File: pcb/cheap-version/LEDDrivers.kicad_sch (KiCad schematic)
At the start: 54 parts, among them J711 LED +/- (return isolated), J721 LED +/- (return isolated), J731 LED +/- (return isolated), Q711 BSC146N10LS5, Q721 BSC146N10LS5, U700 SN74LVC1G08DBVR, U710 AL8853S-13, U720 AL8853S-13

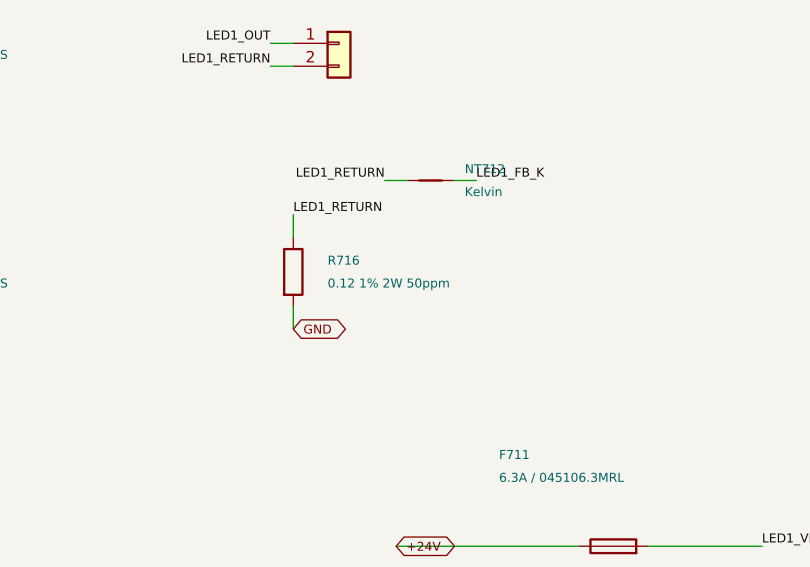
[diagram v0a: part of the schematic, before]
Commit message: Verify cheap-version purchase parts and require complete release checks
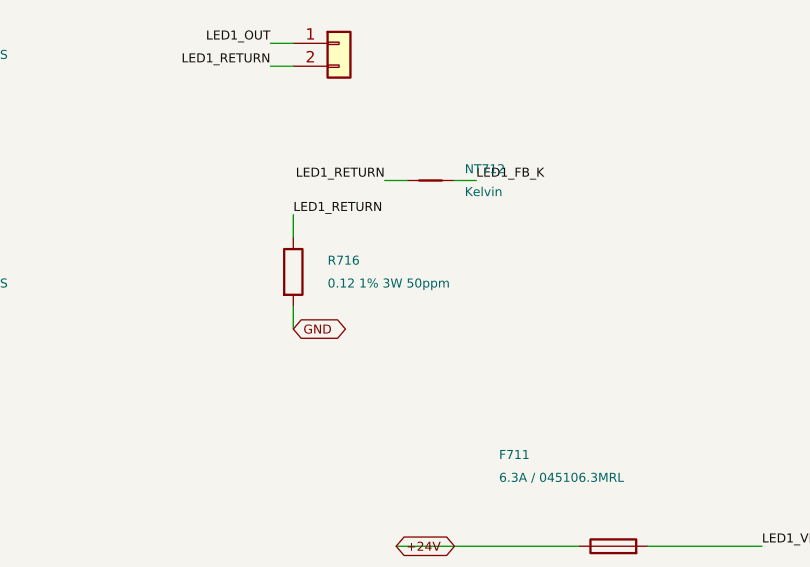
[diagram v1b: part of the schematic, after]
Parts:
- R716: value 0.12 1% 2W 50ppm -> 0.12 1% 3W 50ppm; LCSC (none) -> C49164917; MPN FRM252WFR120TM -> JER2512F3R120; Manufacturer FOJAN -> JIERR; Source (none) -> buy
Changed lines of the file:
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@@
 			)
 		)
-		(property "Value" "0.12 1% 2W 50ppm"
+		(property "Value" "0.12 1% 3W 50ppm"
 			(at 448.31 124.46 0)
 			(show_name no)
@@
 			)
 		)
-		(property "Datasheet" "https://datasheet.lcsc.com/datasheet/pdf/b47da348e6587de9f1f028172ba2b8ea.pdf"
+		(property "Datasheet" "https://datasheet.lcsc.com/datasheet/pdf/02ae4b20613551dea68a63964573e262.pdf"
 			(at 444.5 123.19 0)
 			(hide yes)
@@
 			)
 		)
-		(property "Manufacturer" "FOJAN"
+		(property "Manufacturer" "JIERR"
 			(at 444.5 123.19 0)
 			(hide yes)
@@
 			)
 		)
-		(property "MPN" "FRM252WFR120TM"
+		(property "MPN" "JER2512F3R120"
 			(at 444.5 123.19 0)
 			(hide yes)
@@
 			)
 		)
-		(property "LCSC" ""
+		(property "LCSC" "C49164917"
 			(at 444.5 123.19 0)
 			(hide yes)
@@
 				(justify left)
 			)
+		)
+		(property "Source" "buy"
+			(at 444.5 123.19 0)
+			(effects
+				(font
+					(size 1 1)
+				)
+				(hide yes)
+				(justify left)
+			)
